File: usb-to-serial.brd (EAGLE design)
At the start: 30.1 x 17.8 mm, 16 parts, among them IC1 HT7333, J1 C10418, U1 CH340ESMD

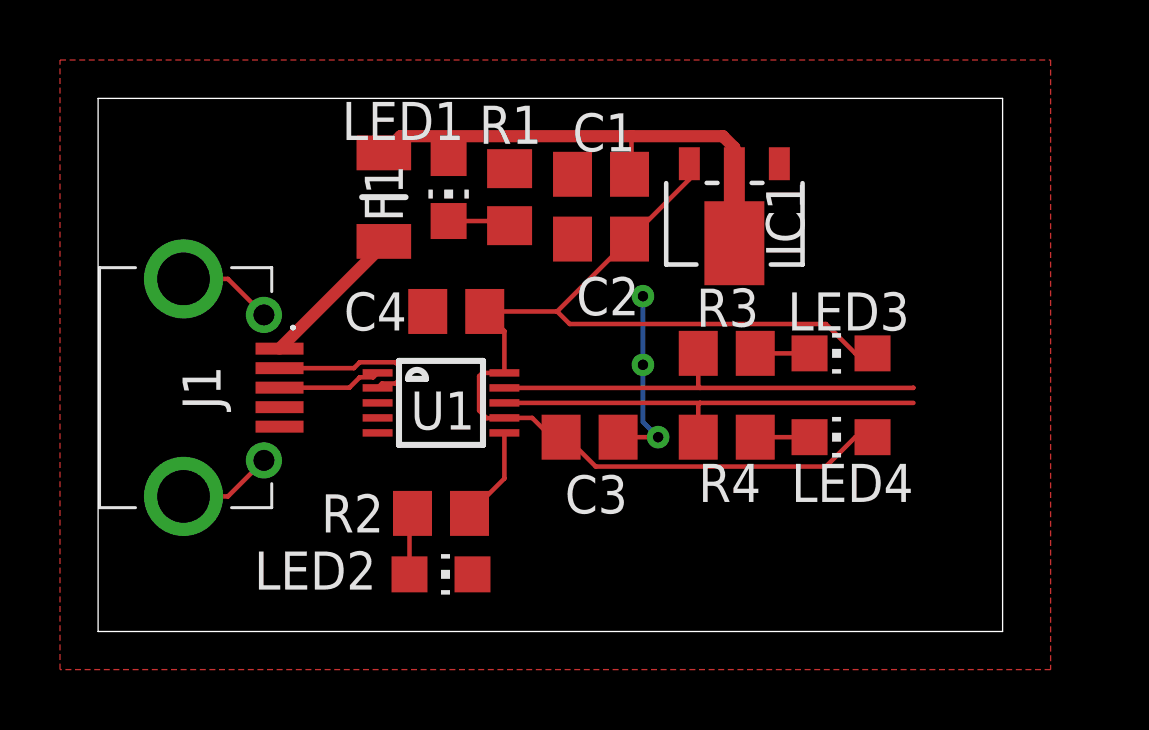
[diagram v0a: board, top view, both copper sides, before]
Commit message: Added pin header
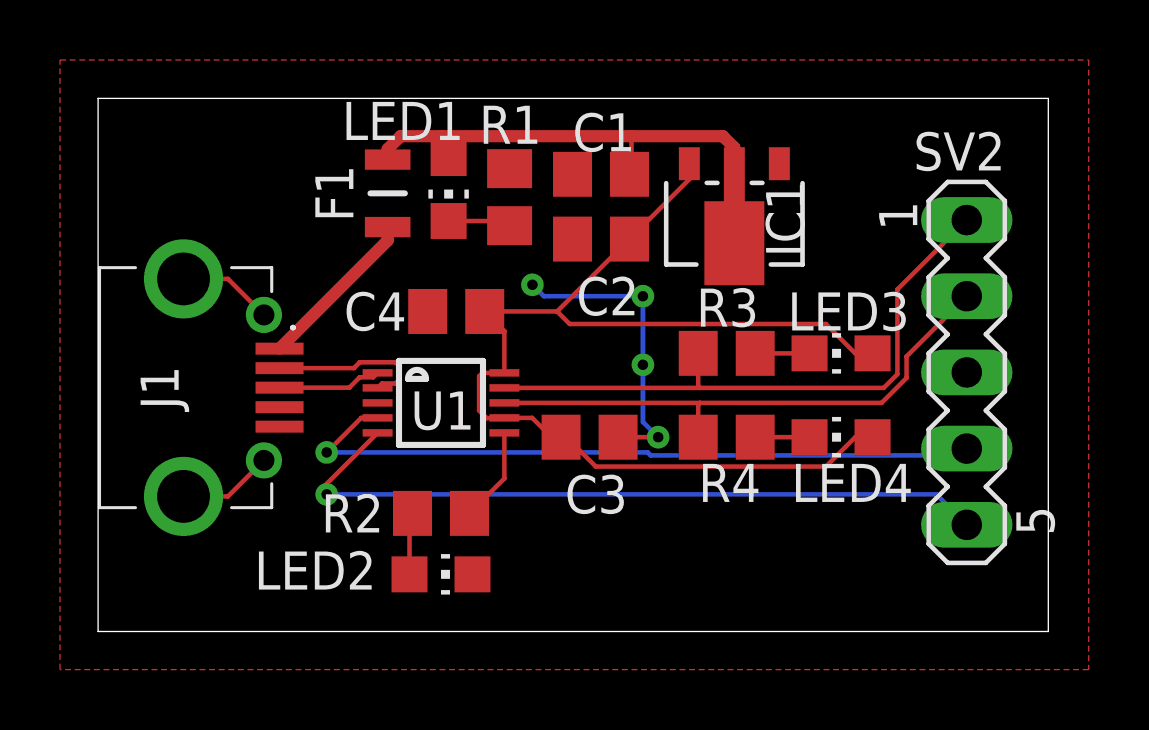
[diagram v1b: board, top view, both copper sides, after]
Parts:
- added SV2: (no value), con-lstb:MA05-1
- F1: value 1206L025YR -> SMD0805-020-16V; device water-lib:FUSC3216X100N -> water-lib:FUSC2114X100N
- moved F1 0.18 mm to (9.65, 14.6)
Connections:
- new net CTS: SV2.5, U1.5
- new net RTS: SV2.4, U1.4
- net GND: now also SV2.3
- net RX: now also SV2.1
- net TX: now also SV2.2
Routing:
- net CTS: track 0.00 -> 24.5 mm, vias 0 -> 1
- net RTS: track 0.00 -> 23.6 mm, vias 0 -> 1
- net RX: track 14.8 -> 20.6 mm
- net GND: track 6.25 -> 10.3 mm, vias 3 -> 4
- net TX: track 14.8 -> 18.5 mm
- net +5V: track 14.3 -> 15.3 mm
- net N$1: track 5.02 -> 5.54 mm
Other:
- board size 30.1 x 17.8 mm -> 31.7 x 17.8 mm
